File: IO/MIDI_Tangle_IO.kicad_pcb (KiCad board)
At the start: 2 copper layers, 40 x 99.5 mm, 102 parts, among them J1 Conn_01x08_Male, J10 AudioJack2_SwitchT, J11 AudioJack2_SwitchT, J12 AudioJack2_SwitchT, J13 AudioJack2_SwitchT, J14 AudioJack2_SwitchT, J15 AudioJack2_SwitchT, J16 AudioJack2_SwitchT, J17 AudioJack2_SwitchT, J18 AudioJack2_SwitchT, J19 AudioJack2_SwitchT, J2 Conn_01x08_Male, J20 AudioJack2_SwitchT, J3 Conn_01x08_Male, J4 Conn_01x08_Male, J5 AudioJack2_SwitchT, J6 AudioJack2_SwitchT, J7 AudioJack2_SwitchT, J8 AudioJack2_SwitchT, J9 AudioJack2_SwitchT, SW1 SW_SPST, SW2 SW_SPST, SW3 SW_SPST, SW4 SW_SPST, SW5 SW_SPST, SW6 SW_SPST, SW7 SW_SPST, SW8 SW_SPST

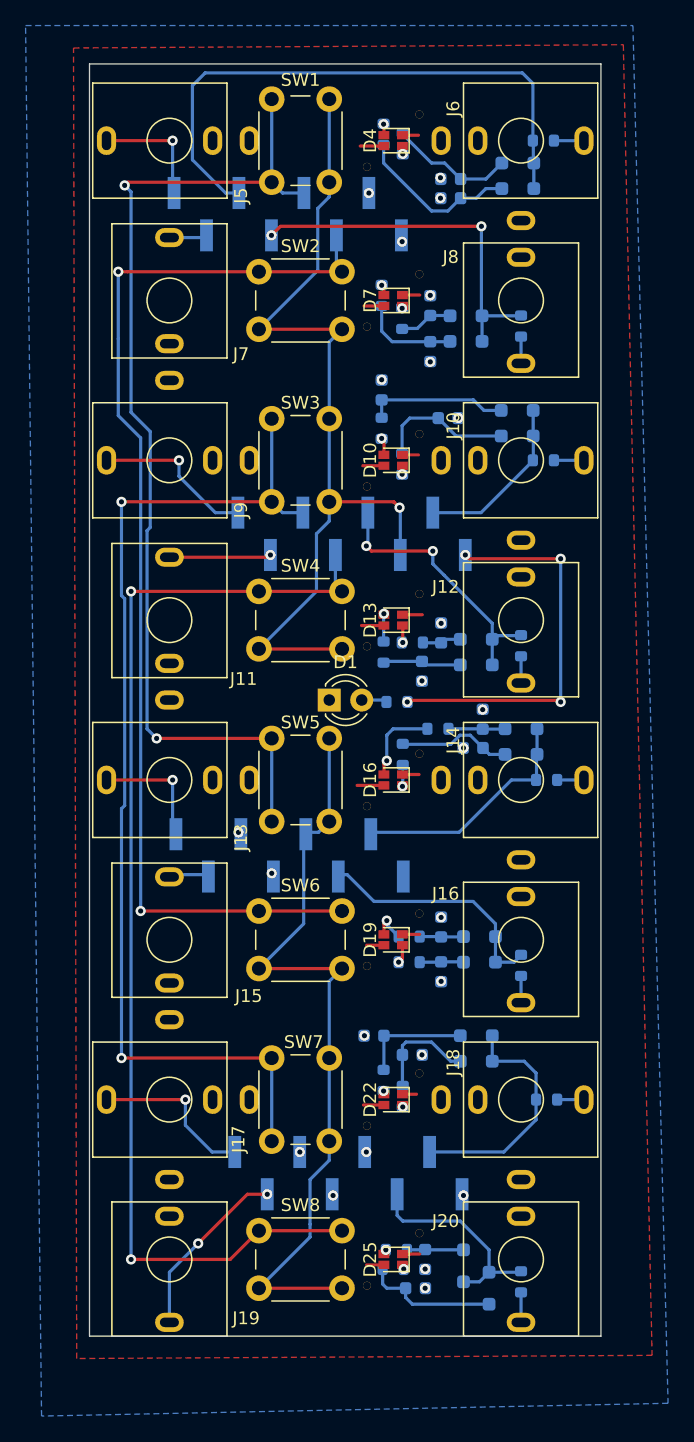
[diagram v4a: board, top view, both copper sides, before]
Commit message: Reduce output capacitive load
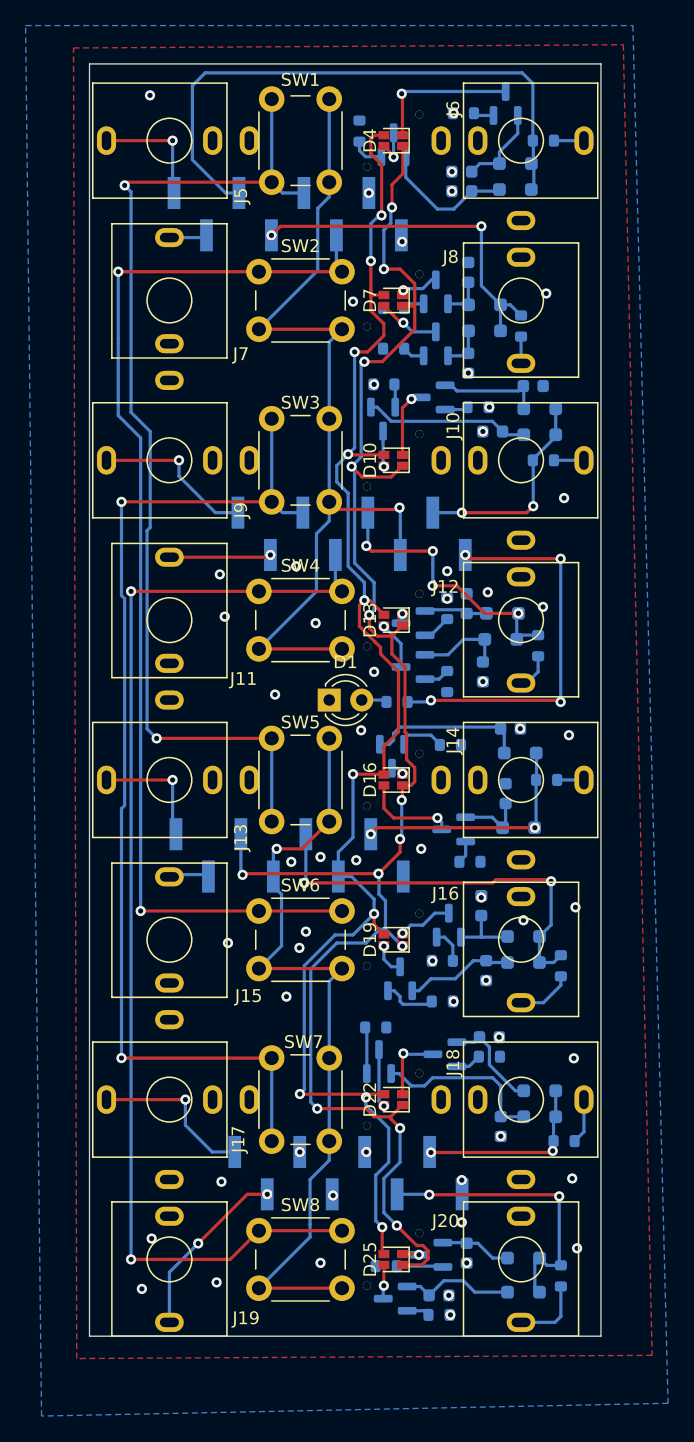
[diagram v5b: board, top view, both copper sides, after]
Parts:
- added Q1: BC847C, Package_TO_SOT_SMD:SOT-23, B.Cu at (82.3, 53.6)
- added Q10: BC857C, Package_TO_SOT_SMD:SOT-23, B.Cu at (76.8, 72.4)
- added Q11: BC857C, Package_TO_SOT_SMD:SOT-23, B.Cu at (72.7, 78.3)
- added Q12: BC857C, Package_TO_SOT_SMD:SOT-23, B.Cu at (75.1, 97.7)
- added Q13: BC857C, Package_TO_SOT_SMD:SOT-23, B.Cu at (78.2, 110.4)
- added Q14: BC857C, Package_TO_SOT_SMD:SOT-23, B.Cu at (74.0, 122.0)
- added Q15: BC857C, Package_TO_SOT_SMD:SOT-23, B.Cu at (72.4, 128.5)
- added Q16: BC857C, Package_TO_SOT_SMD:SOT-23, B.Cu at (73.7, 147.1)
- added Q2: BC847C, Package_TO_SOT_SMD:SOT-23, B.Cu at (76.8, 68.3)
- added Q3: BC847C, Package_TO_SOT_SMD:SOT-23, B.Cu at (76.6, 76.6)
- added Q4: BC847C, Package_TO_SOT_SMD:SOT-23, B.Cu at (75.1, 94.2)
- added Q5: BC847C, Package_TO_SOT_SMD:SOT-23, B.Cu at (73.4, 104.6)
- added Q6: BC847C, Package_TO_SOT_SMD:SOT-23, B.Cu at (77.9, 117.9)
- added Q7: BC847C, Package_TO_SOT_SMD:SOT-23, B.Cu at (77.5, 128.0)
- added Q8: BC847C, Package_TO_SOT_SMD:SOT-23, B.Cu at (76.5, 143.6)
- added Q9: BC857C, Package_TO_SOT_SMD:SOT-23, B.Cu at (73.5, 56.8)
- C1, C10, C11, C12, C13, C14, C15, C16, C2, C3, C4, C5, C6, C7, C8, C9: value 100nF -> 100pF
- R10, R13, R16, R19, R22, R25, R4, R7: value 1k -> 2k
- R12, R15, R18, R21, R24, R3, R6, R9: value 680 -> 2k
- moved C5 11.9 mm to (84.5, 75.7), turned to 0 degrees
- moved R16 9.91 mm to (79.5, 112.9), turned to 0 degrees
- moved C13 9.03 mm to (81.0, 126.6), turned to 0 degrees
- moved C14 8.90 mm to (81.9, 133.6), turned to -90 degrees
- moved R21 8.48 mm to (81.0, 128.1), turned to 0 degrees
- moved R9 7.72 mm to (80.1, 77.3), turned to 0 degrees
- moved C3 6.88 mm to (79.4, 66.8), turned to 90 degrees
- moved D21 6.59 mm to (85.0, 132.8)
- moved D20 6.57 mm to (85.0, 130.8)
- moved R3 6.46 mm to (79.0, 54.4), turned to 180 degrees
- moved R10 6.40 mm to (72.8, 75.6), turned to 180 degrees
- moved C7 6.34 mm to (79.2, 92.7), turned to 90 degrees
- moved R12 6.03 mm to (77.7, 93.1), turned to 90 degrees
- moved R22 5.79 mm to (72.1, 125.9), turned to 0 degrees
- moved D15 5.74 mm to (83.3, 110.2)
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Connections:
- D10 pad 1: Net-(D10-A1) -> +VDC
- D10 pad 2: GND -> Net-(D10-A2)
- D10 pad 3: GND -> Net-(D10-K1)
- D10 pad 4: Net-(D10-K2) -> -VDC
- D13 pad 1: Net-(D13-A1) -> +VDC
- D13 pad 2: GND -> Net-(D13-A2)
- D13 pad 3: GND -> Net-(D13-K1)
- D13 pad 4: Net-(D13-K2) -> -VDC
- D16 pad 1: Net-(D16-A1) -> +VDC
- D16 pad 2: GND -> Net-(D16-A2)
- D16 pad 3: GND -> Net-(D16-K1)
- D16 pad 4: Net-(D16-K2) -> -VDC
- D19 pad 1: Net-(D19-A1) -> +VDC
- D19 pad 2: GND -> Net-(D19-A2)
- D19 pad 3: GND -> Net-(D19-K1)
- D19 pad 4: Net-(D19-K2) -> -VDC
- D22 pad 1: Net-(D22-A1) -> +VDC
- D22 pad 2: GND -> Net-(D22-A2)
- D22 pad 3: GND -> Net-(D22-K1)
- D22 pad 4: Net-(D22-K2) -> -VDC
- D25 pad 1: Net-(D25-A1) -> +VDC
- D25 pad 2: GND -> Net-(D25-A2)
- D25 pad 3: GND -> Net-(D25-K1)
- D25 pad 4: Net-(D25-K2) -> -VDC
- D4 pad 1: Net-(D4-A1) -> +VDC
- D4 pad 2: GND -> Net-(D4-A2)
- D4 pad 3: GND -> Net-(D4-K1)
- D4 pad 4: Net-(D4-K2) -> -VDC
- D7 pad 1: Net-(D7-A1) -> +VDC
- D7 pad 2: GND -> Net-(D7-A2)
- D7 pad 3: GND -> Net-(D7-K1)
- D7 pad 4: Net-(D7-K2) -> -VDC
- J3 pad 3: GND -> -VDC
- J3 pad 4: GND -> ButtSelY
- J3 pad 5: ButtSelY -> JackO6
- J3 pad 6: JackO6 -> +VDC
- R10 pad 1: Net-(D9-A) -> Net-(Q11-E)
- R10 pad 2: Net-(D10-K2) -> GND
- R12 pad 1: Net-(D13-A1) -> Net-(Q4-E)
- R12 pad 2: Net-(D11-K) -> GND
- R13 pad 1: Net-(D12-A) -> Net-(Q12-E)
- R13 pad 2: Net-(D13-K2) -> GND
- R15 pad 1: Net-(D16-A1) -> Net-(Q5-E)
- R15 pad 2: Net-(D14-K) -> GND
- R16 pad 1: Net-(D15-A) -> Net-(Q13-E)
- R16 pad 2: Net-(D16-K2) -> GND
- R18 pad 1: Net-(D19-A1) -> Net-(Q6-E)
- R18 pad 2: Net-(D17-K) -> GND
- R19 pad 1: Net-(D18-A) -> Net-(Q14-E)
- R19 pad 2: Net-(D19-K2) -> GND
- R21 pad 1: Net-(D22-A1) -> Net-(Q7-E)
- R21 pad 2: Net-(D20-K) -> GND
- R22 pad 1: Net-(D21-A) -> Net-(Q15-E)
- R22 pad 2: Net-(D22-K2) -> GND
- R24 pad 1: Net-(D25-A1) -> Net-(Q8-E)
- R24 pad 2: Net-(D23-K) -> GND
- R25 pad 1: Net-(D24-A) -> Net-(Q16-E)
- R25 pad 2: Net-(D25-K2) -> GND
- R3 pad 1: Net-(D4-A1) -> Net-(Q1-E)
- R3 pad 2: Net-(D2-K) -> GND
- R4 pad 1: Net-(D3-A) -> Net-(Q9-E)
- R4 pad 2: Net-(D4-K2) -> GND
- R6 pad 1: Net-(D7-A1) -> Net-(Q2-E)
- R6 pad 2: Net-(D5-K) -> GND
- R7 pad 1: Net-(D6-A) -> Net-(Q10-E)
- R7 pad 2: Net-(D7-K2) -> GND
- R9 pad 1: Net-(D10-A1) -> Net-(Q3-E)
- R9 pad 2: Net-(D8-K) -> GND
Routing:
- net -VDC: track 0.00 -> 135.5 mm, vias 0 -> 13
- net +VDC: track 0.00 -> 118.1 mm, vias 0 -> 10
- net GND: track 23.9 -> 0.18 mm, vias 24 -> 59
- net JackO6: track 19.3 -> 32.0 mm, vias 0 -> 2
- net Net-(D4-K1): track 0.00 -> 11.5 mm, vias 0 -> 1
- net Net-(D14-K): track 4.48 -> 12.4 mm
- net Net-(D16-A2): track 0.00 -> 7.32 mm, vias 0 -> 1
- net Net-(D16-A1): track 6.59 -> 0.00 mm, vias 1 -> 0
- net JackO8: track 16.6 -> 23.1 mm, vias 0 -> 2
- net Net-(D2-K): track 13.0 -> 6.79 mm
- net Net-(D22-K1): track 0.00 -> 5.56 mm, vias 0 -> 1
- net Net-(D10-K1): track 0.00 -> 5.47 mm, vias 0 -> 1
- net Net-(D21-A): track 8.42 -> 13.7 mm
- net Net-(D18-A): track 3.45 -> 8.48 mm
- net Net-(D7-A2): track 0.00 -> 4.90 mm, vias 0 -> 1
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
